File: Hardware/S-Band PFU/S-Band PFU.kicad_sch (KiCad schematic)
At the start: 2 parts, among them U1 LMH5401, U2 LMH5401

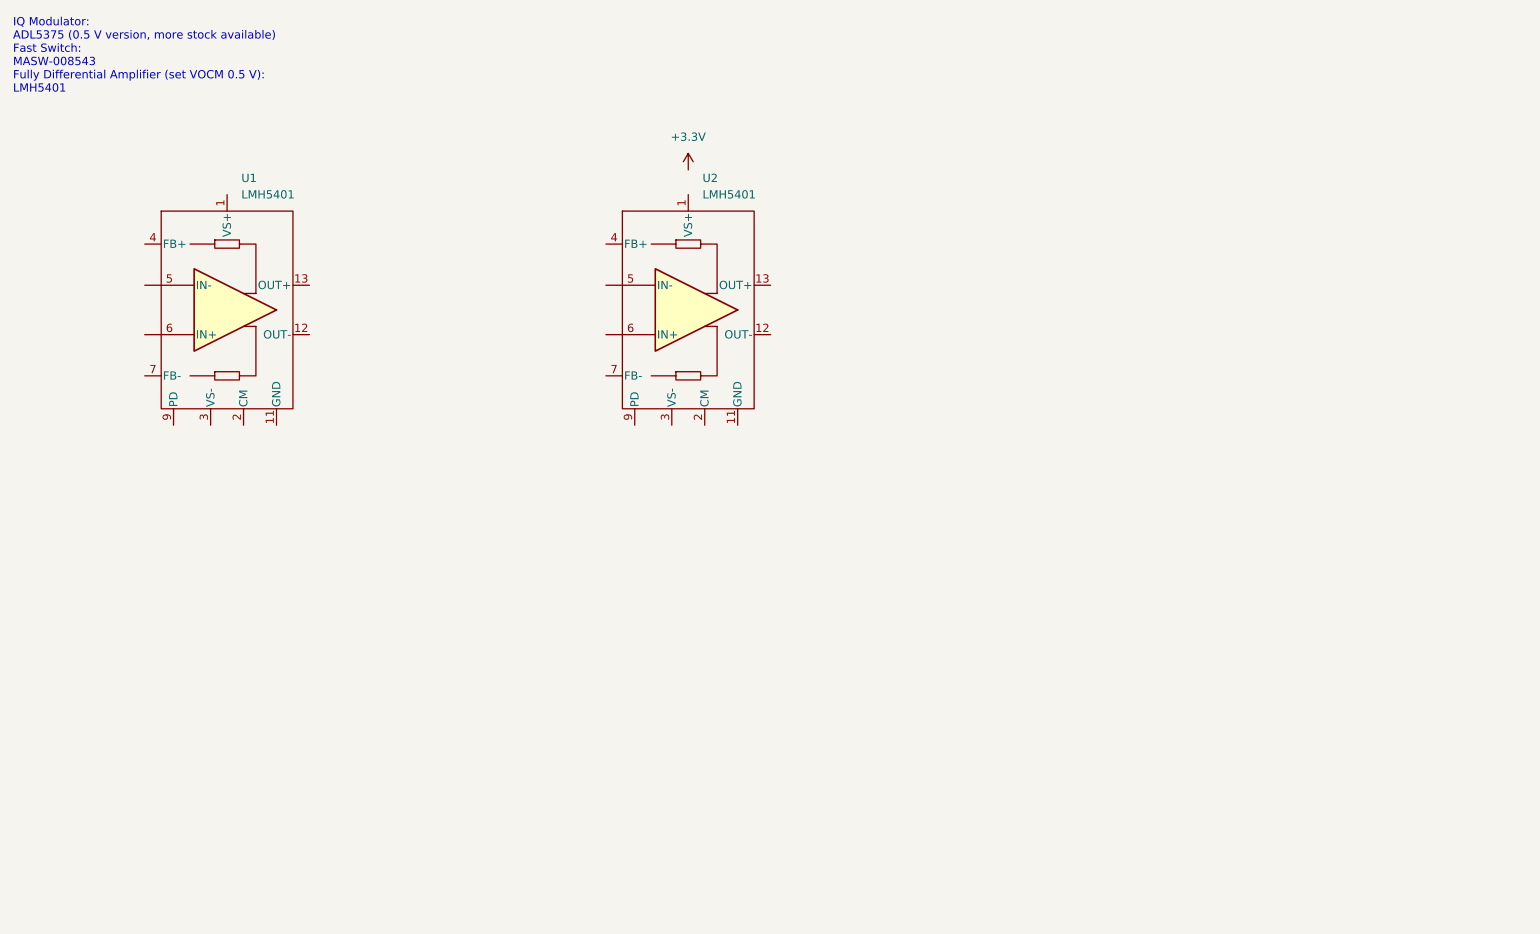
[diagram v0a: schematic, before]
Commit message: Updating schematic for PFU
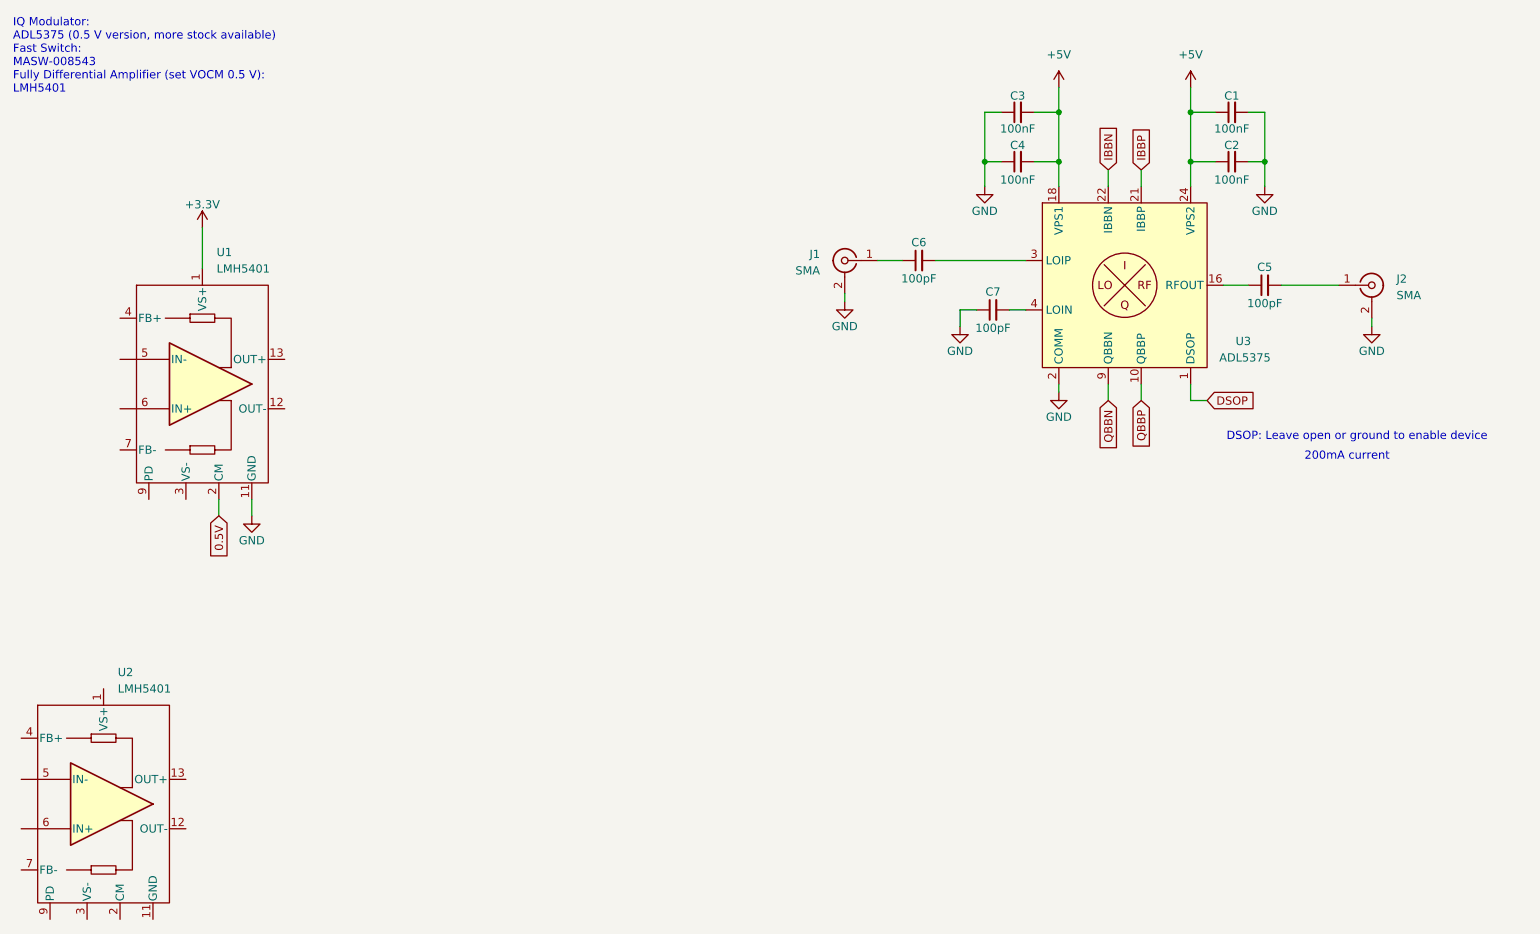
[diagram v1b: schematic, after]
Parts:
- added C1, C2, C3, C4: 100nF, symbol Device:C_Small
- added C5, C6, C7: 100pF, symbol Device:C_Small
- added J1, J2: SMA, symbol Connector:Conn_Coaxial
- added U3: ADL5375, Package_CSP:LFCSP-24-1EP_4x4mm_P0.5mm_EP2.3x2.3mm_ThermalVias, symbol _tim-RF:ADL5375
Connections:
- net VS+ is gone; now on net +3.3V: U1.1 (VS+), U1.10 (VS+), U2.1 (VS+), U2.10 (VS+)
- net 0.5V: now reaches U1.2 (CM)
- net GND renamed COMM
- net COMM: now also C1.2, C2.2, C3.1, C4.1, C7.1, J1.2 (Ext), J2.2 (Ext), U3.11 (COMM), U3.12 (COMM), U3.13 (COMM), U3.14 (COMM), U3.15 (COMM), U3.17 (COMM), U3.19 (COMM), U3.2 (COMM), U3.20 (COMM), U3.23 (COMM), U3.25 (EP), U3.5 (COMM), U3.6 (COMM), U3.7 (COMM), U3.8 (COMM)
- new net: C7.2, U3.4 (LOIN)
- new net: C6.1, J1.1 (In)
- new net: C5.1, U3.16 (RFOUT)
- new net: C5.2, J2.1 (In)
- new net: C6.2, U3.3 (LOIP)
- new net +5V: C1.1, C2.1, C3.2, C4.2, U3.18 (VPS1), U3.24 (VPS2)
- new net DSOP: U3.1 (DSOP)
- new net IBBN: U3.22 (IBBN)
- new net IBBP: U3.21 (IBBP)
- new net QBBN: U3.9 (QBBN)
- new net QBBP: U3.10 (QBBP)
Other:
- note added: "200mA current"
- note added: "DSOP: Leave open or ground to enable device"
- moved on the sheet: U1, U2

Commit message: Updates to schematic
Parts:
- added U4: LMV358, symbol Amplifier_Operational:LMV358
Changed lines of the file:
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@@
+	)
+	(symbol
+		(lib_id "Amplifier_Operational:LMV358")
+		(at 193.04 121.92 0)
+		(unit 2)
+		(exclude_from_sim no)
+		(in_bom yes)
+		(on_board yes)
+		(dnp no)
+		(fields_autoplaced yes)
+		(property "Reference" "U4"
+			(at 193.04 111.76 0)
+			(effects
+				(font
+					(size 1.27 1.27)
+				)
+			)
+		)
+		(property "Value" "LMV358"
+			(at 193.04 114.3 0)
+			(effects
+				(font
+					(size 1.27 1.27)
+				)
+			)
+		)
+		(property "Footprint" ""
+			(at 193.04 121.92 0)
+			(effects
+				(font
+					(size 1.27 1.27)
+				)
+				(hide yes)
+			)
+		)
+		(property "Datasheet" "http://www.ti.com/lit/ds/symlink/lmv324.pdf"
+			(at 193.04 121.92 0)
+			(effects
+				(font
+					(size 1.27 1.27)
+				)
+				(hide yes)
+			)
+		)
+		(property "Description" "Dual Low-Voltage Rail-to-Rail Output Operational Amplifiers, SOIC-8/SSOP-8"
+			(at 193.04 121.92 0)
+			(effects
+				(font
+					(size 1.27 1.27)
+				)
+				(hide yes)
+			)
+		)
+		(pin "1"
+		)
+		(pin "6"
+		)
+		(pin "8"
+		)
+		(pin "5"
+		)
+		(pin "3"
+		)
+		(pin "4"
+		)
+		(pin "2"
+		)
+		(pin "7"
+		)
+		(instances
+			(project "S-Band PFU"
+				(path "/ccc62c73-faa6-4c56-8095-6f1e9dd4cdee"
+					(reference "U4")
+					(unit 2)
+				)
+			)
+		)
 	)
 	(symbol
@@
 	)
 	(symbol
+		(lib_id "Amplifier_Operational:LMV358")
+		(at 214.63 121.92 0)
+		(unit 3)
+		(exclude_from_sim no)
+		(in_bom yes)
+		(on_board yes)
+		(dnp no)
+		(fields_autoplaced yes)
+		(property "Reference" "U4"
+			(at 213.36 120.6499 0)
+			(effects
+				(font
+					(size 1.27 1.27)
+				)
+				(justify left)
+			)
+		)
+		(property "Value" "LMV358"
+			(at 213.36 123.1899 0)
+			(effects
+				(font
+					(size 1.27 1.27)
+				)
+				(justify left)
+			)
+		)
+		(property "Footprint" ""
+			(at 214.63 121.92 0)
+			(effects
+				(font
+					(size 1.27 1.27)
+				)
+				(hide yes)
+			)
+		)
+		(property "Datasheet" "http://www.ti.com/lit/ds/symlink/lmv324.pdf"
+			(at 214.63 121.92 0)
+			(effects
+				(font
+					(size 1.27 1.27)
+				)
+				(hide yes)
+			)
+		)
+		(property "Description" "Dual Low-Voltage Rail-to-Rail Output Operational Amplifiers, SOIC-8/SSOP-8"
+			(at 214.63 121.92 0)
+			(effects
+				(font
+					(size 1.27 1.27)
+				)
+				(hide yes)
+			)
+		)
+		(pin "1"
+		)
+		(pin "6"
+		)
+		(pin "8"
+		)
+		(pin "5"
+		)
+		(pin "3"
+		)
+		(pin "4"
+		)
+		(pin "2"
+		)
+		(pin "7"
+		)
+		(instances
+			(project "S-Band PFU"
+				(path "/ccc62c73-faa6-4c56-8095-6f1e9dd4cdee"
+					(reference "U4")
+					(unit 3)
+				)
+			)
+		)
+	)
+	(symbol
 		(lib_id "power:+3.3V")
 		(at 63.5 54.61 0)
@@
 					(unit 1)
 				)
+			)
+		)
+	)
+	(symbol
+		(lib_id "Amplifier_Operational:LMV358")
+		(at 171.45 121.92 0)
+		(unit 1)
+		(exclude_from_sim no)
+		(in_bom yes)
+		(on_board yes)
+		(dnp no)
+		(fields_autoplaced yes)
+		(property "Reference" "U4"
+			(at 171.45 111.76 0)
+			(effects
+				(font
+					(size 1.27 1.27)
+				)
+			)
+		)
+		(property "Value" "LMV358"
+			(at 171.45 114.3 0)
+			(effects
+				(font
+					(size 1.27 1.27)
+				)
+			)
+		)
+		(property "Footprint" ""
+			(at 171.45 121.92 0)
+			(effects
+				(font
+					(size 1.27 1.27)
+				)
+				(hide yes)
+			)
+		)
+		(property "Datasheet" "http://www.ti.com/lit/ds/symlink/lmv324.pdf"
+			(at 171.45 121.92 0)
+			(effects
+				(font
+					(size 1.27 1.27)
+				)
+				(hide yes)
+			)
+		)
+		(property "Description" "Dual Low-Voltage Rail-to-Rail Output Operational Amplifiers, SOIC-8/SSOP-8"
+			(at 171.45 121.92 0)
+			(effects
+				(font
+					(size 1.27 1.27)
+				)
+				(hide yes)
+			)
+		)
+		(pin "1"
+		)
+		(pin "6"
+		)
+		(pin "8"
+		)
+		(pin "5"
+		)
+		(pin "3"
+		)
+		(pin "4"
+		)
+		(pin "2"
+		)
+		(pin "7"
+		)
+		(instances
+			(project "S-Band PFU"
+				(path "/ccc62c73-faa6-4c56-8095-6f1e9dd4cdee"
+					(reference "U4")
+					(unit 1)
+				)
